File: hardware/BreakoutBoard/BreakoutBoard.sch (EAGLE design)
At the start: 67 parts, among them J1 CON-71436-2164-TOP, J2 CON-71439-2164, J3 CON-2X8-RASTER, J4 CON-2X8-RASTER, J5 CON-2X8-RASTER, J6 CON-2X8-RASTER, J7 CON-HTST-105-04-D-RA, M1 MOUNT-HOLE3.3, M2 MOUNT-HOLE3.3, M3 MOUNT-HOLE3.3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

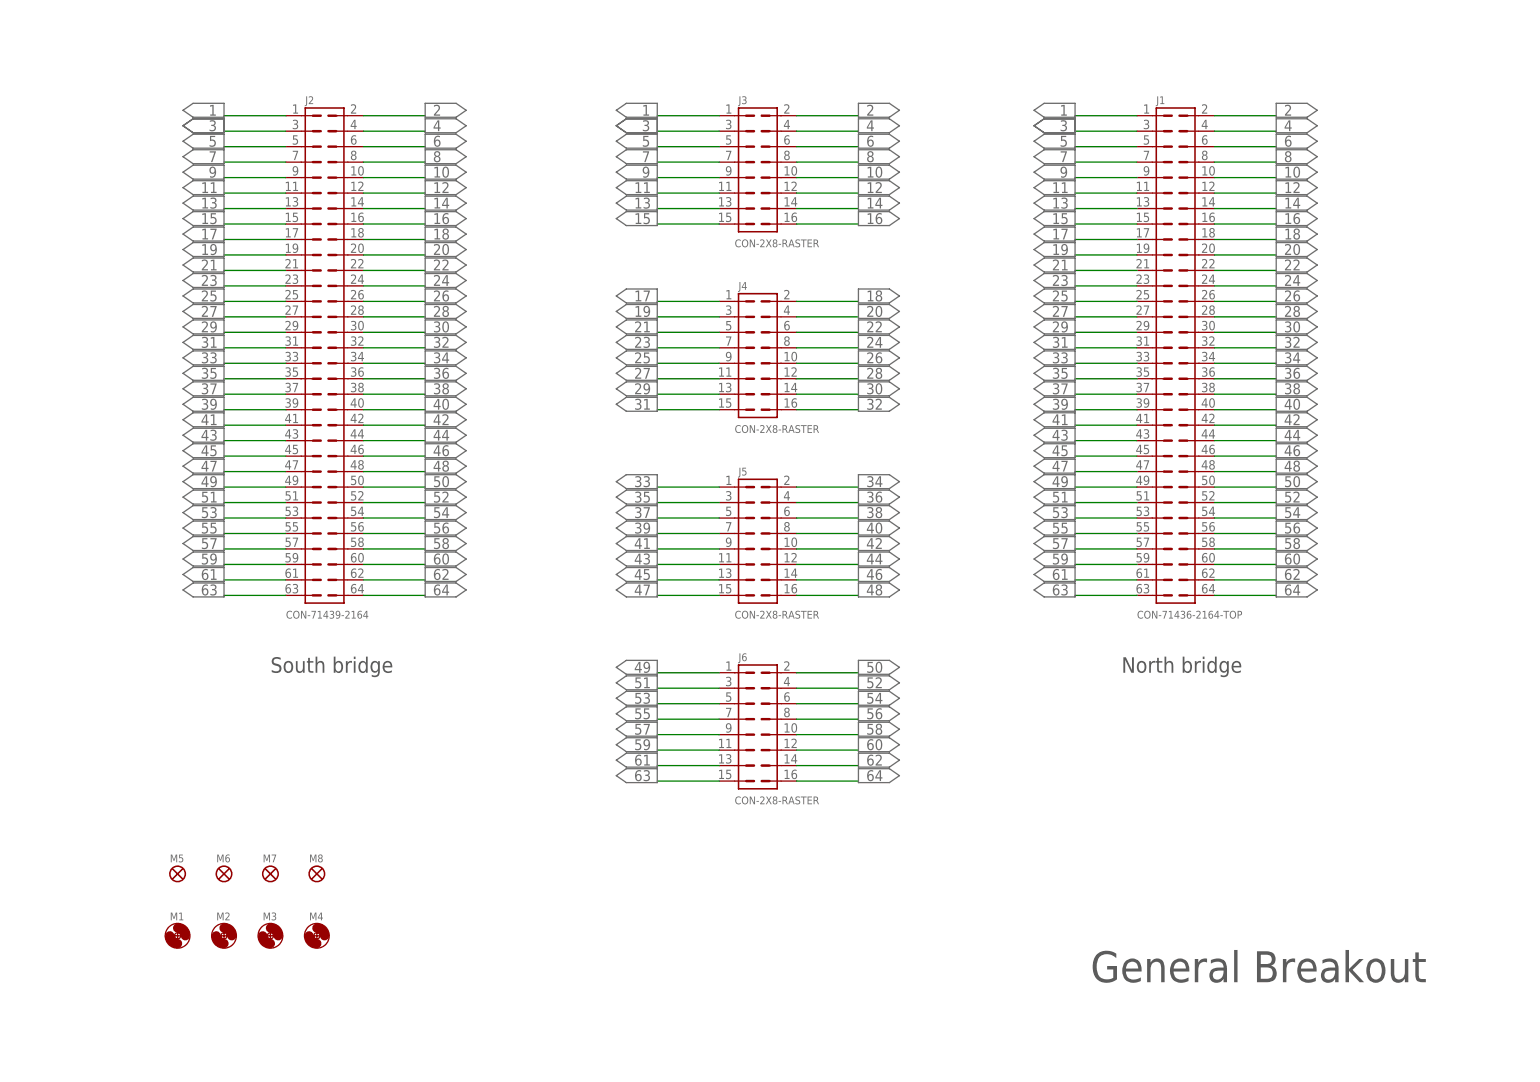
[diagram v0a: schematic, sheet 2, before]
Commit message: - 64 -> 84 board-to-board connector, initial changes
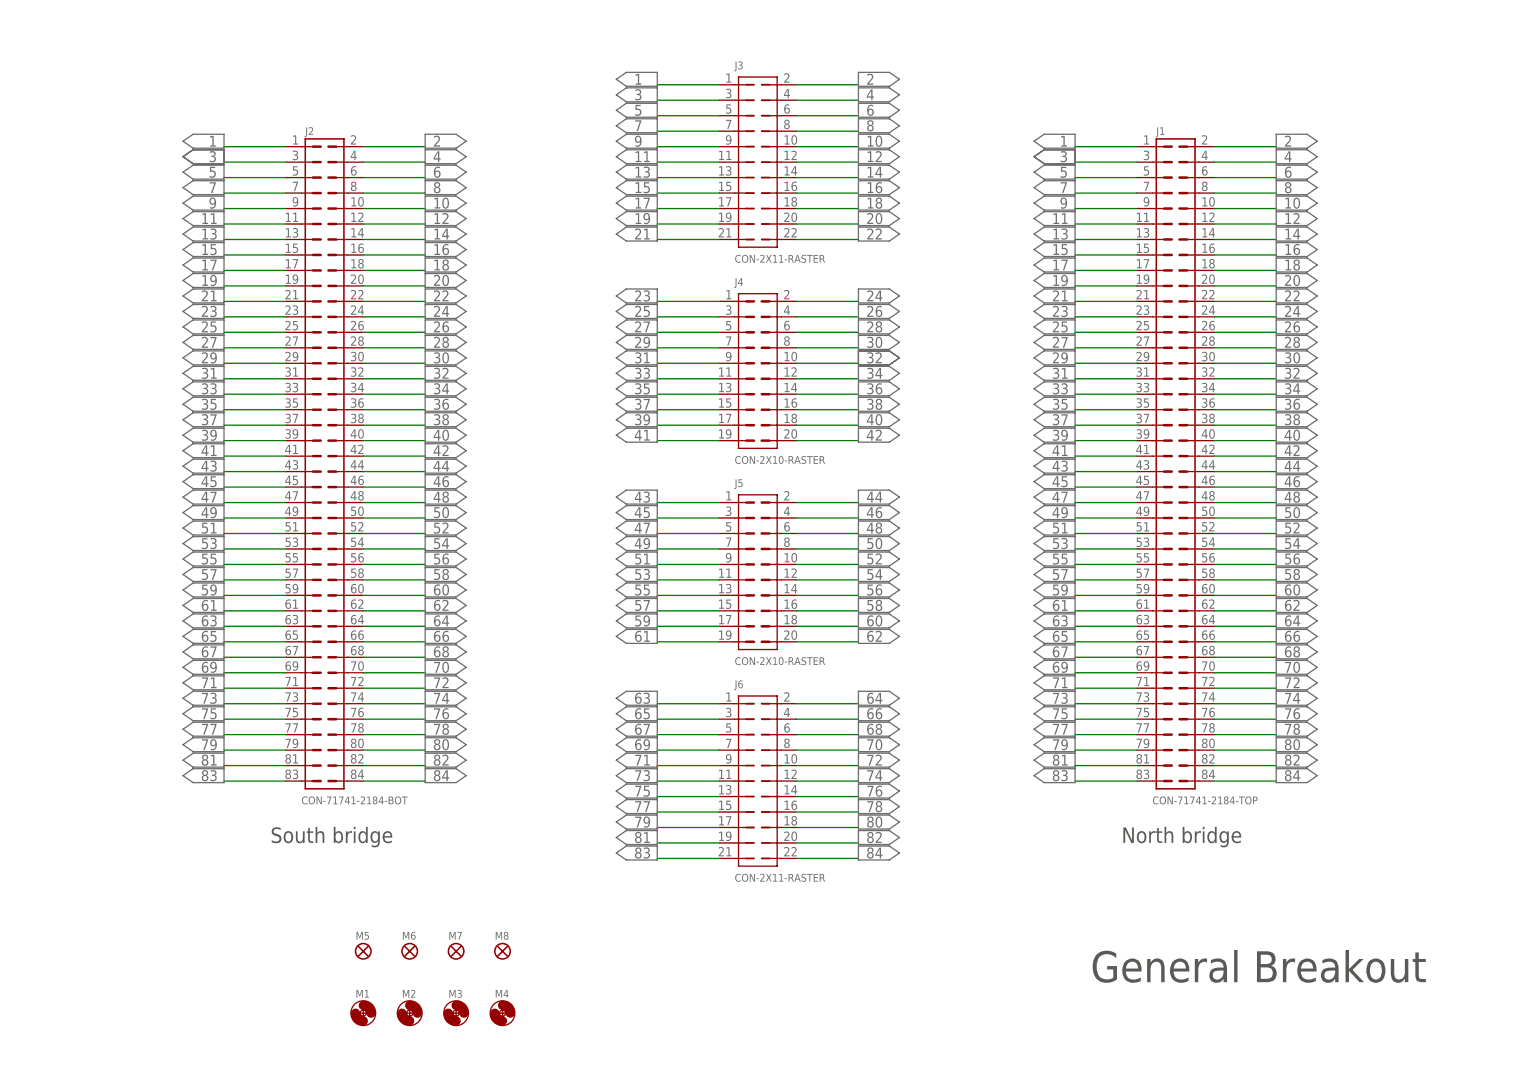
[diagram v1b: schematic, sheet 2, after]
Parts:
- J1: value CON-71436-2164-TOP -> CON-71741-2184-TOP; device BreakoutBoard:CON-71436-2164-TOP -> BreakoutBoard:CON-71741-2184-TOP
- J2: value CON-71439-2164 -> CON-71741-2184-BOT; device BreakoutBoard:CON-71439-2164 -> BreakoutBoard:CON-71741-2184-BOT
- J3, J6: value CON-2X8-RASTER -> CON-2X11-RASTER; device BreakoutBoard:CON-2X8-RASTER -> BreakoutBoard:CON-2X11-RASTER
- J4, J5: value CON-2X8-RASTER -> CON-2X10-RASTER; device BreakoutBoard:CON-2X8-RASTER -> BreakoutBoard:CON-2X10-RASTER
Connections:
- new net 65: J1.65, J2.65, J6.3
- new net 66: J1.66, J2.66, J6.4
- new net 67: J1.67, J2.67, J6.5
- new net 68: J1.68, J2.68, J6.6
- new net 69: J1.69, J2.69, J6.7
- new net 70: J1.70, J2.70, J6.8
- new net 71: J1.71, J2.71, J6.9
- new net 72: J1.72, J2.72, J6.10
- new net 73: J1.73, J2.73, J6.11
- new net 74: J1.74, J2.74, J6.12
- new net 75: J1.75, J2.75, J6.13
- new net 76: J1.76, J2.76, J6.14
- new net 77: J1.77, J2.77, J6.15
- new net 78: J1.78, J2.78, J6.16
- new net 79: J1.79, J2.79, J6.17
- new net 80: J1.80, J2.80, J6.18
- new net 81: J1.81, J2.81, J6.19
- new net 82: J1.82, J2.82, J6.20
- new net 83: J1.83, J2.83, J6.21
- new net 84: J1.84, J2.84, J6.22
- net 17: now also J3.17; no longer J4.1
- net 18: now also J3.18; no longer J4.2
- net 19: now also J3.19; no longer J4.3
- net 20: now also J3.20; no longer J4.4
- net 21: now also J3.21; no longer J4.5
- net 22: now also J3.22; no longer J4.6
- net 23: now also J4.1; no longer J4.7
- net 24: now also J4.2; no longer J4.8
- net 25: now also J4.3; no longer J4.9
- net 26: now also J4.4; no longer J4.10
- net 27: now also J4.5; no longer J4.11
- net 28: now also J4.6; no longer J4.12
- net 29: now also J4.7; no longer J4.13
- net 30: now also J4.8; no longer J4.14
- net 31: now also J4.9; no longer J4.15
- net 32: now also J4.10; no longer J4.16
- net 33: now also J4.11; no longer J5.1
- net 34: now also J4.12; no longer J5.2
- net 35: now also J4.13; no longer J5.3
- net 36: now also J4.14; no longer J5.4
- net 37: now also J4.15; no longer J5.5
- net 38: now also J4.16; no longer J5.6
- net 39: now also J4.17; no longer J5.7
- net 40: now also J4.18; no longer J5.8
- net 41: now also J4.19; no longer J5.9
- net 42: now also J4.20; no longer J5.10
- net 43: now also J5.1; no longer J5.11
- net 44: now also J5.2; no longer J5.12
- net 45: now also J5.3; no longer J5.13
- net 46: now also J5.4; no longer J5.14
- net 47: now also J5.5; no longer J5.15
- net 48: now also J5.6; no longer J5.16
- net 49: now also J5.7; no longer J6.1
- net 50: now also J5.8; no longer J6.2
- net 51: now also J5.9; no longer J6.3
- net 52: now also J5.10; no longer J6.4
- net 53: now also J5.11; no longer J6.5
- net 54: now also J5.12; no longer J6.6
- net 55: now also J5.13; no longer J6.7
- net 56: now also J5.14; no longer J6.8
- net 57: now also J5.15; no longer J6.9
- net 58: now also J5.16; no longer J6.10
- net 59: now also J5.17; no longer J6.11
- net 60: now also J5.18; no longer J6.12
- net 61: now also J5.19; no longer J6.13
- net 62: now also J5.20; no longer J6.14
- net 63: now also J6.1; no longer J6.15
- net 64: now also J6.2; no longer J6.16
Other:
- moved on the sheet: M1, M2, M3, M4, M5, M6, M7, M8

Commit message: - Routing and layout
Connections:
- net 60: no longer R16.1, TP7.1
- net 62: no longer R21.1, TP9.1
- net 63: no longer R33.1
- net 64: no longer R34.1
- net 80: now also R16.1, TP7.1
- net 82: now also R21.1, TP9.1
- net 83: now also R33.1
- net 84: now also R34.1
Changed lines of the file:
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@@
 <setting verticaltext="up"/>
 </settings>
-<grid distance="0.1" unitdist="inch" unit="inch" style="lines" multiple="1" display="no" altdistance="0.05" altunitdist="inch" altunit="inch"/>
+<grid distance="0.1" unitdist="inch" unit="inch" style="lines" multiple="1" display="no" altdistance="0.01" altunitdist="inch" altunit="inch"/>
 <layers>
 <layer number="1" name="Top" color="4" fill="1" visible="no" active="no"/>
@@
 <attribute name="PAGE2" value="General Breakout"/>
 <attribute name="PAGE3" value="Power Board Specific"/>
+<attribute name="REVIEWER" value="Peter Volgyesi"/>
+<attribute name="REVIEWEREMAIL" value="peter.volgyesi@vanderbilt.edu"/>
 <attribute name="REVISION" value="B"/>
 <attribute name="TITLE" value="Breakout Board"/>
-<attribute name="VERIFIER" value="Peter Volgyesi"/>
-<attribute name="VERIFIEREMAIL" value="peter.volgyesi@vanderbilt.edu"/>
 </attributes>
 <variantdefs>
@@
 <parts>
 <part name="FRAME5" library="powerboard" deviceset="FRAME-LETTER" device=""/>
-<part name="AUTHOR-FIELD" library="powerboard" deviceset="FRATME-AUTHOR-FIELD" device=""/>
 <part name="TOC-FIELD" library="BreakoutBoard" deviceset="FRAME-TOC" device=""/>
 <part name="LOGO1" library="Logo" deviceset="LOGO-ISIS-600MIL" device="-10MM-AU"/>
@@
 <part name="PORT149" library="BreakoutBoard" deviceset="PORT2" device=""/>
 <part name="J6" library="BreakoutBoard" deviceset="CON-2X11-RASTER" device=""/>
+<part name="U$14" library="BreakoutBoard" deviceset="FRAME-AUTHOR-FIELD" device=""/>
 </parts>
 <sheets>
@@
 <text x="161.29" y="20.32" size="2.54" layer="95" rot="MR0">&gt;AUTHOREMAIL</text>
 <text x="85.09" y="20.32" size="2.54" layer="95">&gt;AUTHOR</text>
-<text x="85.09" y="5.08" size="2.54" layer="95">&gt;VERIFIER</text>
-<text x="161.29" y="5.08" size="2.54" layer="95" rot="MR0">&gt;VERIFIEREMAIL</text>
+<text x="85.09" y="5.08" size="2.54" layer="95">&gt;REVIEWER</text>
+<text x="161.29" y="5.08" size="2.54" layer="95" rot="MR0">&gt;REVIEWEREMAIL</text>
 </plain>
 <instances>
 <instance part="FRAME5" gate="G$1" x="0" y="0"/>
 <instance part="FRAME5" gate="G$2" x="147.32" y="0"/>
-<instance part="AUTHOR-FIELD" gate="G$1" x="81.28" y="0"/>
 <instance part="TOC-FIELD" gate="G$1" x="0" y="0"/>
 <instance part="LOGO1" gate="G$1" x="104.14" y="60.96"/>
@@
 <instance part="LOGO3" gate="G$1" x="129.54" y="60.96"/>
 <instance part="LOGO4" gate="G$1" x="154.94" y="60.96"/>
+<instance part="U$14" gate="G$1" x="81.28" y="0"/>
 </instances>
 <busses>
@@
 </segment>
 </net>
-<net name="60" class="0">
-<segment>
-<wire x1="152.4" y1="149.86" x2="157.48" y2="149.86" width="0.1524" layer="91"/>
-<wire x1="157.48" y1="149.86" x2="162.56" y2="149.86" width="0.1524" layer="91"/>
-<wire x1="157.48" y1="154.94" x2="157.48" y2="149.86" width="0.1524" layer="91"/>
-<junction x="157.48" y="149.86"/>
-<label x="144.78" y="149.86" size="1.778" layer="95"/>
-<pinref part="R16" gate="G$1" pin="1"/>
-<pinref part="TP7" gate="G$1" pin="1"/>
-</segment>
-</net>
-<net name="62" class="0">
-<segment>
-<wire x1="157.48" y1="109.22" x2="162.56" y2="109.22" width="0.1524" layer="91"/>
-<wire x1="157.48" y1="114.3" x2="157.48" y2="109.22" width="0.1524" layer="91"/>
-<wire x1="157.48" y1="109.22" x2="152.4" y2="109.22" width="0.1524" layer="91"/>
-<junction x="157.48" y="109.22"/>
-<label x="144.78" y="109.22" size="1.778" layer="95"/>
-<pinref part="R21" gate="G$1" pin="1"/>
-<pinref part="TP9" gate="G$1" pin="1"/>
-</segment>
-</net>
 <net name="2" class="0">
 <segment>
@@
 <label x="73.66" y="25.4" size="1.778" layer="95"/>
 <pinref part="R32" gate="G$1" pin="1"/>
-</segment>
-</net>
-<net name="64" class="0">
-<segment>
-<wire x1="119.38" y1="25.4" x2="114.3" y2="25.4" width="0.1524" layer="91"/>
-<label x="109.22" y="25.4" size="1.778" layer="95"/>
-<pinref part="R34" gate="G$1" pin="1"/>
 </segment>
 </net>
@@
 </segment>
 </net>
-<net name="63" class="0">
+<net name="1" class="0">
+<segment>
+<wire x1="83.82" y1="33.02" x2="78.74" y2="33.02" width="0.1524" layer="91"/>
+<label x="73.66" y="33.02" size="1.778" layer="95"/>
+<pinref part="R31" gate="G$1" pin="1"/>
+</segment>
+</net>
+<net name="80" class="0">
+<segment>
+<wire x1="152.4" y1="149.86" x2="157.48" y2="149.86" width="0.1524" layer="91"/>
+<wire x1="157.48" y1="149.86" x2="162.56" y2="149.86" width="0.1524" layer="91"/>
+<wire x1="157.48" y1="154.94" x2="157.48" y2="149.86" width="0.1524" layer="91"/>
+<junction x="157.48" y="149.86"/>
+<label x="144.78" y="149.86" size="1.778" layer="95"/>
+<pinref part="R16" gate="G$1" pin="1"/>
+<pinref part="TP7" gate="G$1" pin="1"/>
+</segment>
+</net>
+<net name="82" class="0">
+<segment>
+<wire x1="157.48" y1="109.22" x2="162.56" y2="109.22" width="0.1524" layer="91"/>
+<wire x1="157.48" y1="114.3" x2="157.48" y2="109.22" width="0.1524" layer="91"/>
+<wire x1="157.48" y1="109.22" x2="152.4" y2="109.22" width="0.1524" layer="91"/>
+<junction x="157.48" y="109.22"/>
+<label x="144.78" y="109.22" size="1.778" layer="95"/>
+<pinref part="R21" gate="G$1" pin="1"/>
+<pinref part="TP9" gate="G$1" pin="1"/>
+</segment>
+</net>
+<net name="83" class="0">
 <segment>
 <wire x1="119.38" y1="33.02" x2="114.3" y2="33.02" width="0.1524" layer="91"/>
@@
 </segment>
 </net>
-<net name="1" class="0">
-<segment>
-<wire x1="83.82" y1="33.02" x2="78.74" y2="33.02" width="0.1524" layer="91"/>
-<label x="73.66" y="33.02" size="1.778" layer="95"/>
-<pinref part="R31" gate="G$1" pin="1"/>
-</segment>
-</net>
+<net name="84" class="0">
+<segment>
+<wire x1="119.38" y1="25.4" x2="114.3" y2="25.4" width="0.1524" layer="91"/>
+<label x="109.22" y="25.4" size="1.778" layer="95"/>
+<pinref part="R34" gate="G$1" pin="1"/>
+</segment>
+</net>

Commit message: - New connectors added and routed
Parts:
- removed R1, R11, R14, R16, R19, R21, R24, R4, R6, R9: 10, BreakoutBoard:R0805
- removed R10, R15, R20, R25, R5: 1000, BreakoutBoard:TRIMMER
- removed R12, R13, R17, R18, R2, R22, R23, R26, R27, R28, R29, R3, R30, R7, R8: 0, BreakoutBoard:R0805
- removed TP10, TP8: TESTPOINT-GREEN, BreakoutBoard:TESTPOINT-GREEN
- removed TP2, TP4, TP6: TESTPOINT-BLUE, BreakoutBoard:TESTPOINT-BLUE
- added J10, J11, J12, J8, J9: CON-2X3-RASTER, BreakoutBoard:CON-2X3-RASTER
- added J13: CON-2X4-RASTER, BreakoutBoard:CON-2X4-RASTER
- J3: value CON-2X11-RASTER -> CON-2X4-RASTER; device BreakoutBoard:CON-2X11-RASTER -> BreakoutBoard:CON-2X4-RASTER
- J5: value CON-2X10-RASTER -> CON-2X3-RASTER; device BreakoutBoard:CON-2X10-RASTER -> BreakoutBoard:CON-2X3-RASTER
- J6: value CON-2X11-RASTER -> CON-2X3-RASTER; device BreakoutBoard:CON-2X11-RASTER -> BreakoutBoard:CON-2X3-RASTER
- J7: value CON-HTST-105-04-D-RA -> CON-2X3-RASTER; device BreakoutBoard:CON-HTST-105-04-D-RA -> BreakoutBoard:CON-2X3-RASTER
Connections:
- removed net A1V5-: R16.2, R17.1, R18.1, TP8.1
- removed net A3V3-: R21.2, R22.1, R23.1, TP10.1
- removed net D1V5-: R11.2, R12.1, R13.1, TP6.1
- removed net D3V3-: R6.2, R7.1, R8.1, TP4.1
- removed net N$10: R17.2, R20.A
- removed net N$11: R22.2, R25.A
- removed net N$13: R2.2, R5.A
- removed net N$14: R3.2, R4.1
- removed net N$15: R13.2, R14.1
- removed net N$16: R23.2, R24.1
- removed net N$4: R10.A, R7.2
- removed net N$5: R8.2, R9.1
- removed net N$8: R12.2, R15.A
- removed net N$9: R18.2, R19.1
- removed net NC: J7.4
- removed net TCK: J7.1, R26.2
- removed net TDI: J7.9, R29.2
- removed net TDO: J7.3, R27.2
- removed net TMS: J7.5, R28.2
- removed net TRST: J7.8, R30.1
- removed net VJTAG: J7.6
- removed net VPUMP: J7.7
- removed net VSUP-: R1.2, R2.1, R3.1, TP2.1
- net 10: now also J4.2; no longer J3.10
- net 11: now also J4.3; no longer J3.11
- net 12: now also J4.4; no longer J3.12
- net 13: now also J4.5; no longer J3.13
- net 14: now also J4.6; no longer J3.14
- net 15: now also J4.7; no longer J3.15
- net 16: now also J4.8; no longer J3.16
- net 17: now also J4.9; no longer J3.17
- net 18: now also J4.10; no longer J3.18
- net 19: now also J4.11; no longer J3.19
- net 20: now also J4.12; no longer J3.20
- net 21: now also J4.13; no longer J3.21
- net 22: now also J4.14; no longer J3.22
- net 23: now also J4.15; no longer J4.1
- net 24: now also J4.16; no longer J4.2
- net 25: now also J4.17; no longer J4.3
- net 26: now also J4.18; no longer J4.4
- net 27: now also J4.19; no longer J4.5
- net 28: now also J4.20; no longer J4.6
- net 29: now also J5.1; no longer J4.7
- net 30: now also J5.2; no longer J4.8, R29.1
- net 31: now also J5.3; no longer J4.9
- net 32: now also J5.4; no longer J4.10, R28.1
- net 33: now also J5.5; no longer J4.11
- net 34: now also J5.6; no longer J4.12, R27.1
- net 35: now also J6.1; no longer J4.13
- net 36: now also J6.2; no longer J4.14, R26.1
- net 37: now also J6.3; no longer J4.15
- net 38: now also J6.4; no longer J4.16, R30.2
- net 39: now also J6.5; no longer J4.17
- net 4: no longer R1.1
- net 40: now also J6.6; no longer J4.18
- net 41: now also J7.1; no longer J4.19
- net 42: now also J7.2; no longer J4.20
- net 43: now also J7.3; no longer J5.1
- net 44: now also J7.4; no longer J5.2
- net 45: now also J7.5; no longer J5.3
- net 46: now also J7.6; no longer J5.4
- net 47: now also J8.1; no longer J5.5
- net 48: now also J8.2; no longer J5.6
- net 49: now also J8.3; no longer J5.7
- net 50: now also J8.4; no longer J5.8
- net 51: now also J8.5; no longer J5.9
- net 52: now also J8.6; no longer J5.10
- net 53: now also J9.1; no longer J5.11
- net 54: now also J9.2; no longer J5.12
- net 55: now also J9.3; no longer J5.13
- net 56: now also J9.4; no longer J5.14
- net 57: now also J9.5; no longer J5.15
- net 58: now also J9.6; no longer J5.16
- net 59: now also J10.1; no longer J5.17
- net 6: no longer R6.1
- net 60: now also J10.2; no longer J5.18
- net 61: now also J10.3; no longer J5.19
- net 62: now also J10.4; no longer J5.20
- net 63: now also J10.5; no longer J6.1
- net 64: now also J10.6; no longer J6.2
- net 65: now also J11.1; no longer J6.3
- net 66: now also J11.2; no longer J6.4
- net 67: now also J11.3; no longer J6.5
- net 68: now also J11.4; no longer J6.6
- net 69: now also J11.5; no longer J6.7
- net 70: now also J11.6; no longer J6.8
- net 71: now also J12.1; no longer J6.9
- net 72: now also J12.2; no longer J6.10
- net 73: now also J12.3; no longer J6.11
- net 74: now also J12.4; no longer J6.12
- net 75: now also J12.5; no longer J6.13
- net 76: now also J12.6; no longer J6.14
- net 77: now also J13.1; no longer J6.15
- net 78: now also J13.2; no longer J6.16
- net 79: now also J13.3; no longer J6.17
- net 8: no longer R11.1
- net 80: now also J13.4; no longer J6.18, R16.1
- net 81: now also J13.5; no longer J6.19
- net 82: now also J13.6; no longer J6.20, R21.1
- net 83: now also J13.7; no longer J6.21
- net 84: now also J13.8; no longer J6.22
- net 9: now also J4.1; no longer J3.9
- net AGND: no longer R19.2, R20.B, R24.2, R25.B
- net DGND: no longer J7.10, J7.2, R10.B, R14.2, R15.B, R4.2, R5.B, R9.2
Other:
- note removed: "A1V5"
- note removed: "A3V3"
- note removed: "D1V5"
- note removed: "D3V3"
- note removed: "GND"
- note removed: "VSUP"
- moved on the sheet: J1, J2, J4

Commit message: - Logos - Gerber files - Pick and Place file - Assembly Drawings
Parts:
- removed LOGO2: LOGO-VANDERBILT-600MIL-10MM-AU, Logo:LOGO-VANDERBILT-600MIL-10MM-AU
- removed LOGO3: LOGO-MARMOTE-600MIL-10MM-AU, Logo:LOGO-MARMOTE-600MIL-10MM-AU
- removed LOGO4: LOGO-MAGNIFYING-GLASS-600MIL-10MM-AU, Logo:LOGO-MAGNIFYING-GLASS-600MIL-10MM-AU
- added LOGO5: LOGO-VANDERBILT-600MIL-10MM-SS, Logo:LOGO-VANDERBILT-600MIL-10MM-SS
- added LOGO6: LOGO-ISIS-600MIL-10MM-SS, Logo:LOGO-ISIS-600MIL-10MM-SS
- added LOGO7: LOGO-MARMOTE-600MIL-10MM-SS, Logo:LOGO-MARMOTE-600MIL-10MM-SS
- LOGO1: value LOGO-ISIS-600MIL-10MM-AU -> LOGO-MAGNIFYING-GLASS-600MIL-10MM-SS; device Logo:LOGO-ISIS-600MIL-10MM-AU -> Logo:LOGO-MAGNIFYING-GLASS-600MIL-10MM-SS
